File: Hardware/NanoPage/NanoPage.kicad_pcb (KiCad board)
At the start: 6 copper layers, 91.8 x 37.5 mm, 92 parts, among them J1 TYPE-C-31-M-12, J2 Micro_SD_Card_Det, J3 FPC-05FB-24PH20, J4 BM03B-SRSS-TB, J5 SM02B-SRSS-TB_LF, Q1 Si1308EDL, U1 USBLC6-2SC6, U2 TPS2116DRLR, U3 BQ25170DSGR, U4 MAX17055ETB+T, U5 PCF85063ATL, U6 TPS22929D, U7 TPS7A0233DBVR, U8 E73-2G4M08S1C, Y1 32.768kHz, Y2 32.768kHz

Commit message: fix: Fix wrong footprint
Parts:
- FL1: footprint Personal library:L_CommonModeChoke_TDK_0503USB -> Personal Library:L_CommonModeChoke_TDK_0503USB
- J3: footprint Personal library:XUNPU FPC-05FB-24PH20 -> Personal Library:XUNPU FPC-05FB-24PH20
- J4: footprint BM03B-SRSS-TB(LF)(SN):BM03BSRSSTBLFSN -> BM03B-SRSS-TB:BM03BSRSSTBLFSN
- J5: footprint SM02B-SRSS-TB(LF)(SN):SM02BSRSSTBLFSN -> SM02B-SRSS-TB:SM02BSRSSTBLFSN
- L1: footprint Personal library:NR4018 -> Personal Library:NR4018
- S4: value SKRPACE010 -> RESET_BTN; footprint SKRPARE010:SKRPARE010 -> PTS526SM15SMTR2:PTS526SM15SMTR2LFS
- U2: footprint TPS2116:SOTFL50P160X60-8N -> TPS2116DRL:SOTFL50P160X60-8N
- U3: footprint Personal library:BQ25170 -> Personal Library:BQ25170
- U4: footprint MAX17055ETB+T:SON40P250X200X80-11N -> MAX17055ETB-T:SON40P250X200X80-11N
- U8: footprint Personal library:E73-2G4M08S1C -> E73-2G4M08S1C:E73-2G4M08S1C
- moved R20 20.9 mm to (156.3, 118.2)
- moved R26 17.6 mm to (113.5, 95.3), turned to 90 degrees
- moved R27 17.6 mm to (114.8, 95.3), turned to 90 degrees
- moved C27 16.8 mm to (116.8, 95.5)
- moved C28 10.7 mm to (123.1, 109.2)
- moved U7 9.51 mm to (133.1, 110.7)
- moved C3 9.51 mm to (133.3, 107.5)
- moved C4 9.51 mm to (136.0, 111.1)
- moved Y2 8.40 mm to (124.9, 108.2), turned to -90 degrees
- moved L2 7.60 mm to (122.4, 100.5), turned to -90 degrees
- moved C29 6.69 mm to (123.1, 107.2), turned to 90 degrees
- moved S4 6.01 mm to (132.1, 102.5), turned to 0 degrees
- moved C13 5.32 mm to (126.3, 100.2)
- moved R18 5.31 mm to (126.3, 102.5)
- moved R14 3.87 mm to (113.7, 112.9)
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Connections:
- U8 pad 1: /Buttons/NEXT_BTN -> /Microcontroller/MCU_SD_ON
- U8 pad 12: /Display/EPD_BUSY -> /Display/EPD_CS
- U8 pad 14: /Display/EPD_RES -> /Display/EPD_DC
- U8 pad 15: /Display/EPD_DC -> /Display/EPD_RES
- U8 pad 16: /Display/EPD_CS -> /Display/EPD_BUSY
- U8 pad 2: /Battery Charger and Fuel Gauge/FUEL_ALERT -> unconnected-(U8-P1.10-Pad2)
- U8 pad 3: /Buttons/ACTION_BTN -> /Battery Charger and Fuel Gauge/CHG_STAT
- U8 pad 33: /Battery Charger and Fuel Gauge/SDA -> /Battery Charger and Fuel Gauge/FUEL_ALERT
- U8 pad 34: /Battery Charger and Fuel Gauge/CHG_STAT -> unconnected-(U8-P0.22-Pad34)
- U8 pad 35: /Battery Charger and Fuel Gauge/SCL -> /Buttons/PREV_BTN
- U8 pad 4: unconnected-(U8-P0.28/AIN4-Pad4) -> /Battery Charger and Fuel Gauge/SCL
- U8 pad 41: /Microcontroller/MCU_RTC_INT -> /Buttons/ACTION_BTN
- U8 pad 43: /Microcontroller/MCU_SD_ON -> /Buttons/NEXT_BTN
- U8 pad 6: unconnected-(U8-P1.13-Pad6) -> /Battery Charger and Fuel Gauge/SDA
- U8 pad 7: /Buttons/PREV_BTN -> /Microcontroller/MCU_RTC_INT
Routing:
- net /Microcontroller/MCU_SWCLK: track 45.4 -> 28.0 mm
- net /Microcontroller/MCU_SWDIO: track 43.9 -> 31.2 mm
- net VBUS: track 72.1 -> 61.2 mm
- net /SD Card/DAT2: track 17.9 -> 7.36 mm
- net /Display/MOSI: track 81.9 -> 72.2 mm, vias 3 -> 2
- net /Display/SCLK: track 82.9 -> 73.8 mm, vias 3 -> 2
- net /Battery Charger and Fuel Gauge/CHG_STAT: track 61.6 -> 70.5 mm
- net +3V3: track 56.0 -> 47.7 mm, vias 19 -> 23
- net /Battery Charger and Fuel Gauge/SCL: track 77.2 -> 69.7 mm
- net /Microcontroller/MISO: track 40.7 -> 33.4 mm, vias 2 -> 0
- net VOUT: track 32.2 -> 39.2 mm
- net /Display/EPD_RES: track 67.4 -> 60.5 mm
- net /Microcontroller/MCU_RTC_INT: track 15.0 -> 8.29 mm, vias 2 -> 0
- net /Display/EPD_DC: track 60.0 -> 66.7 mm
- net /Battery Charger and Fuel Gauge/FUEL_ALERT: track 59.5 -> 53.6 mm
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
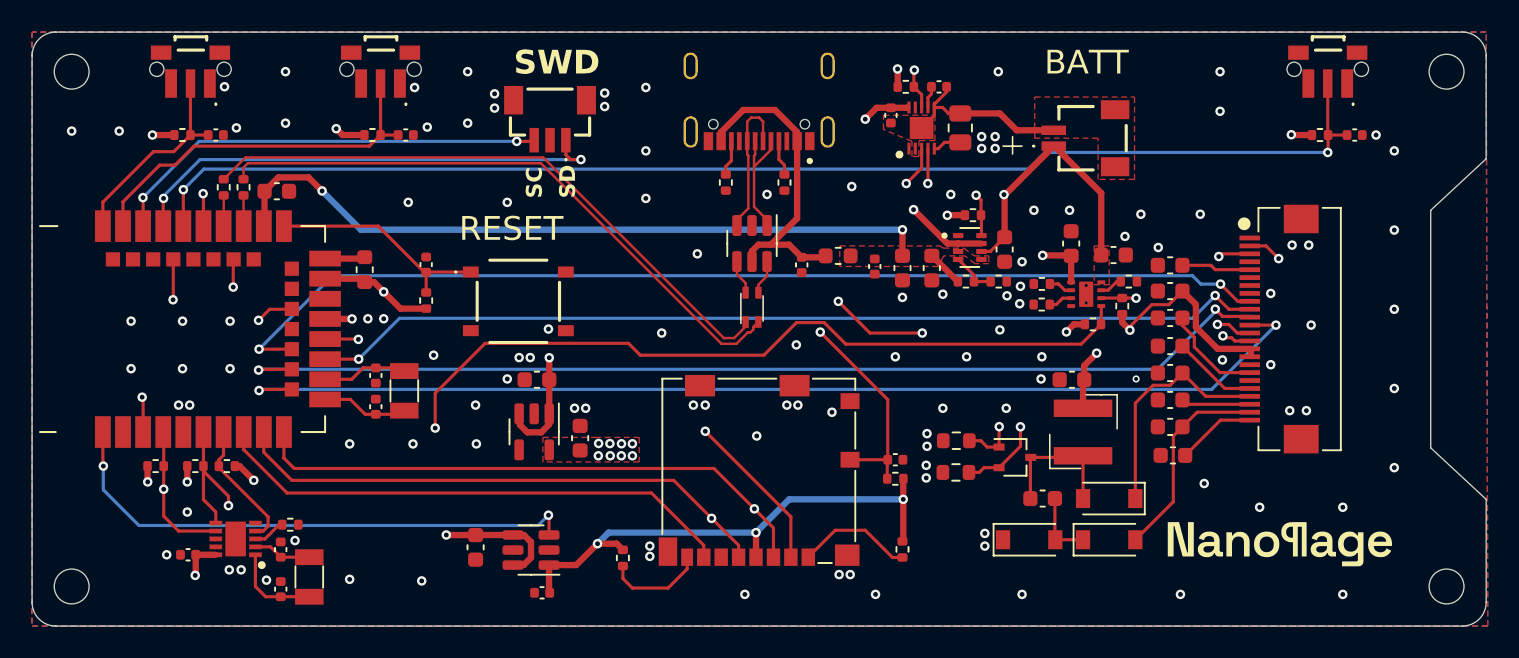
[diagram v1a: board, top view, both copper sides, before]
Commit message: feat: Add an external button connector and fix some issues
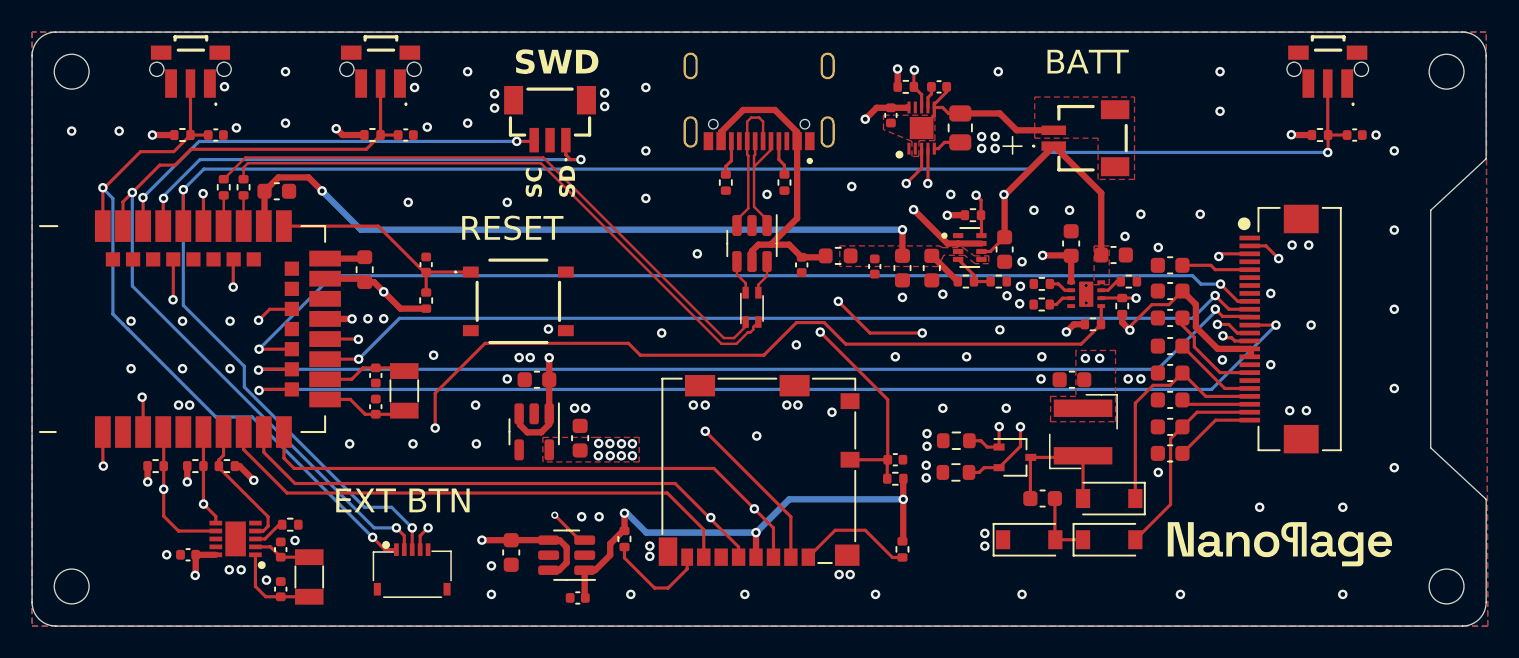
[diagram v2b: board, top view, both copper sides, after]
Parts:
- added J6: Conn_01x07, Personal Library:HC-FPC-05-09-5RLTAG, F.Cu at (125.4, 119.7)
- moved C14 2.27 mm to (131.7, 118.4)
- moved C15 2.27 mm to (135.8, 121.2)
- moved U6 2.27 mm to (135.2, 118.5)
- moved R19 1.20 mm to (138.8, 117.5)
- moved C26 0.22 mm to (173.2, 112.1)
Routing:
- net /Buttons/NEXT_BTN: track 13.2 -> 46.0 mm, vias 0 -> 2
- net /Buttons/ACTION_BTN: track 23.9 -> 54.4 mm, vias 0 -> 2
- net /Buttons/PREV_BTN: track 81.1 -> 110.8 mm, vias 2 -> 3
- net +3V3: track 47.7 -> 45.6 mm, vias 23 -> 25
- net +3V3_SD: track 33.1 -> 31.4 mm
- net /Battery Charger and Fuel Gauge/SDA: track 68.1 -> 66.4 mm
- net /Microcontroller/MISO: track 33.4 -> 34.0 mm
- net GND: vias 119 -> 122
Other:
- board text added: "EXT BTN"
